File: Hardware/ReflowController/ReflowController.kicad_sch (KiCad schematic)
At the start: 4 parts, among them J1 Conn_01x03_Socket

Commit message: updated main schematic with kerem
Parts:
- removed J1: Conn_01x03_Socket, symbol Connector:Conn_01x03_Socket
- added J10, J11, J3, J4, J5, J6, J7, J8, J9: 2060-1452, 810_connectors_clable_to_Board:wago_2060-1452, symbol Connector:Conn_01x02_Socket
- added J12: RJ45_Display, Connector_RJ:RJ45_Amphenol_54602-x08_Horizontal, symbol Connector:RJ45
- added J13: RJ45_Keypad, Connector_RJ:RJ45_Amphenol_54602-x08_Horizontal, symbol Connector:RJ45
- added J14: Conn_01x03_Socket, 810_connectors_clable_to_Board:wago_2060-1453, symbol Connector:Conn_01x03_Socket
- gave numbers to parts that had none: 3
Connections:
- net PSU/+24V_IN: now also J11.1 (Pin_1)
- net PSU/24V_GND_IN: now also J11.2 (Pin_2)
- net TemperatureReader/PT100_+IN: now also J14.2 (Pin_2)
- net TemperatureReader/PT100_+OUT: now also J14.1 (Pin_1)
- net TemperatureReader/PT100_-IN: now also J14.3 (Pin_3)
- new net Fan Driver/FAN_1_OUT_+: J9.1 (Pin_1)
- new net Fan Driver/FAN_1_OUT_-: J9.2 (Pin_2)
- new net Fan Driver/FAN_2_OUT_+: J10.1 (Pin_1)
- new net Fan Driver/FAN_2_OUT_-: J10.2 (Pin_2)
- new net IO/HSS_1_OUT_+: J3.1 (Pin_1)
- new net IO/HSS_1_OUT_-: J3.2 (Pin_2)
- new net IO/HSS_2_OUT_+: J4.1 (Pin_1)
- new net IO/HSS_2_OUT_-: J5.2 (Pin_2)
- new net IO/HSS_3_OUT_+: J6.1 (Pin_1)
- new net IO/HSS_3_OUT_-: J4.2 (Pin_2)
- new net IO/HSS_4_OUT_+: J5.1 (Pin_1)
- new net IO/HSS_4_OUT_-: J6.2 (Pin_2)
- new net IO/relay_1_coil_+: J7.1 (Pin_1)
- new net IO/relay_1_coil_-: J7.2 (Pin_2)
- new net IO/relay_2_coil_+: J8.1 (Pin_1)
- new net IO/relay_2_coil_-: J8.2 (Pin_2)
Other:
- sheet Fan Driver ports: added +24V, +5V, FAN_1_OUT_+, FAN_1_OUT_-, FAN_2_OUT_+, FAN_2_OUT_-, GND, MOTOR_A_EN, MOTOR_A_PWM, MOTOR_B_EN, MOTOR_B_PWM, PGND; removed FAN+, FAN-
- sheet IO ports: added +3.3V, HSS_1_IN, HSS_1_OUT_+, HSS_1_OUT_-, HSS_1_STATUS, HSS_2_IN, HSS_2_OUT_+, HSS_2_OUT_-, HSS_2_STATUS, HSS_3_IN, HSS_3_OUT_+, HSS_3_OUT_-, HSS_3_STATUS, HSS_4_IN, HSS_4_OUT_+, HSS_4_OUT_-, HSS_4_STATUS, HSS_STATUS_DIS, relay_1_coil_+, relay_1_coil_-, relay_1_in, relay_2_coil_+, relay_2_coil_-, relay_2_in; removed none
- title: (none) -> Reflow Oven Control

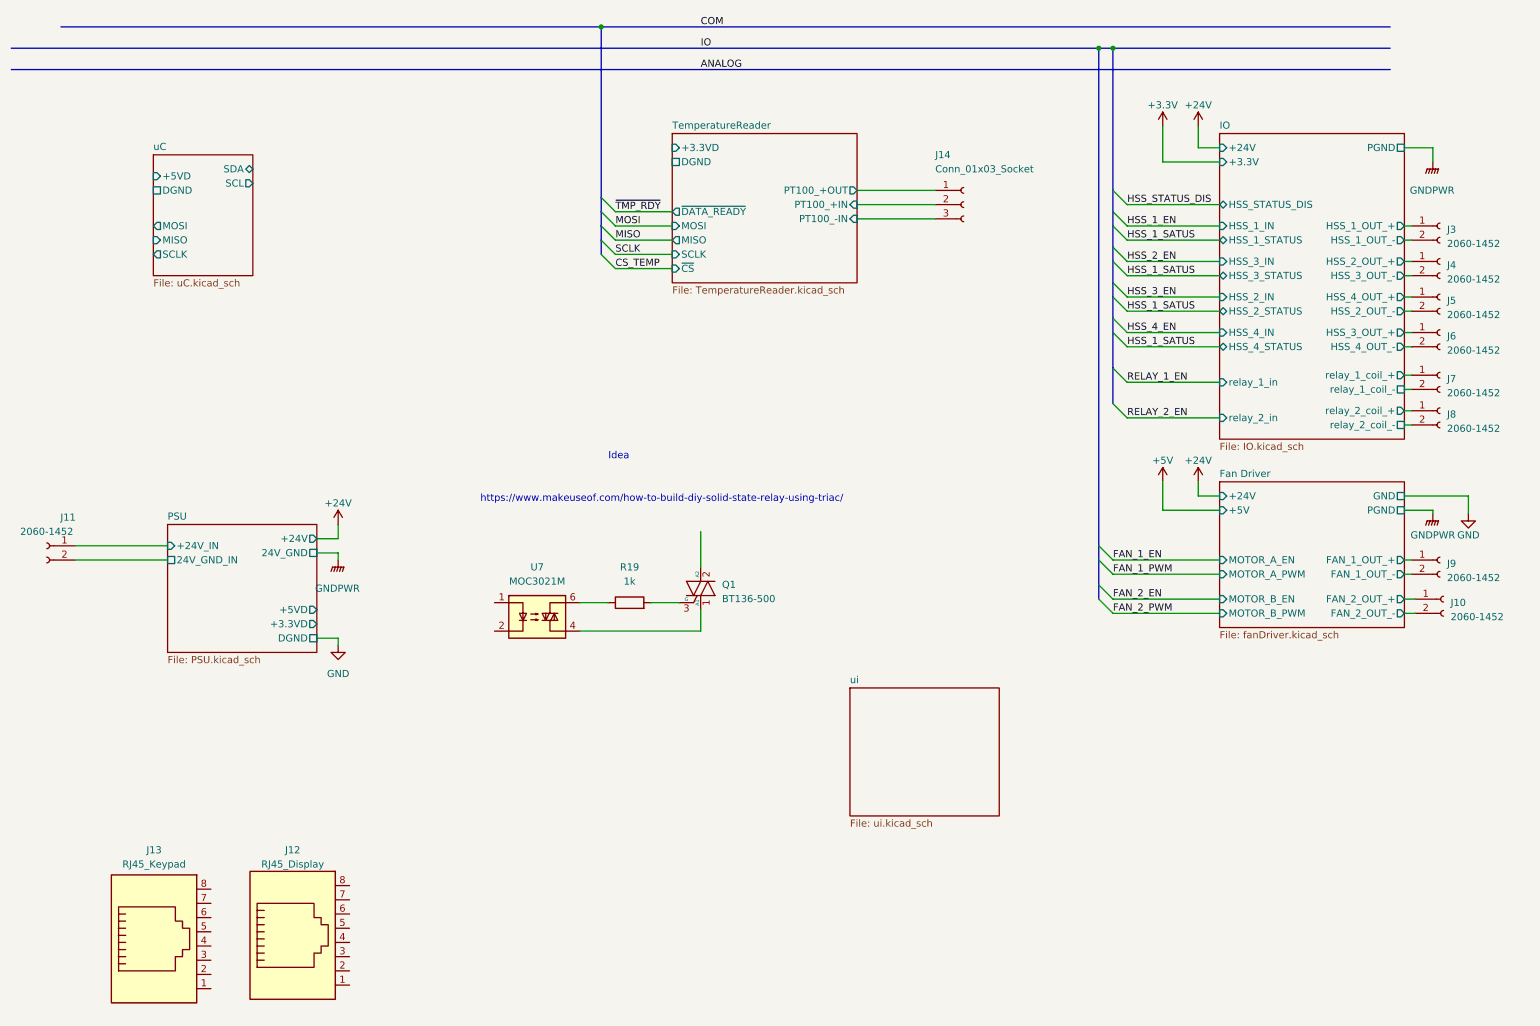
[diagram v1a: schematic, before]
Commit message: added the schematic of the updated pwerAndUi branch(with uC schematic update
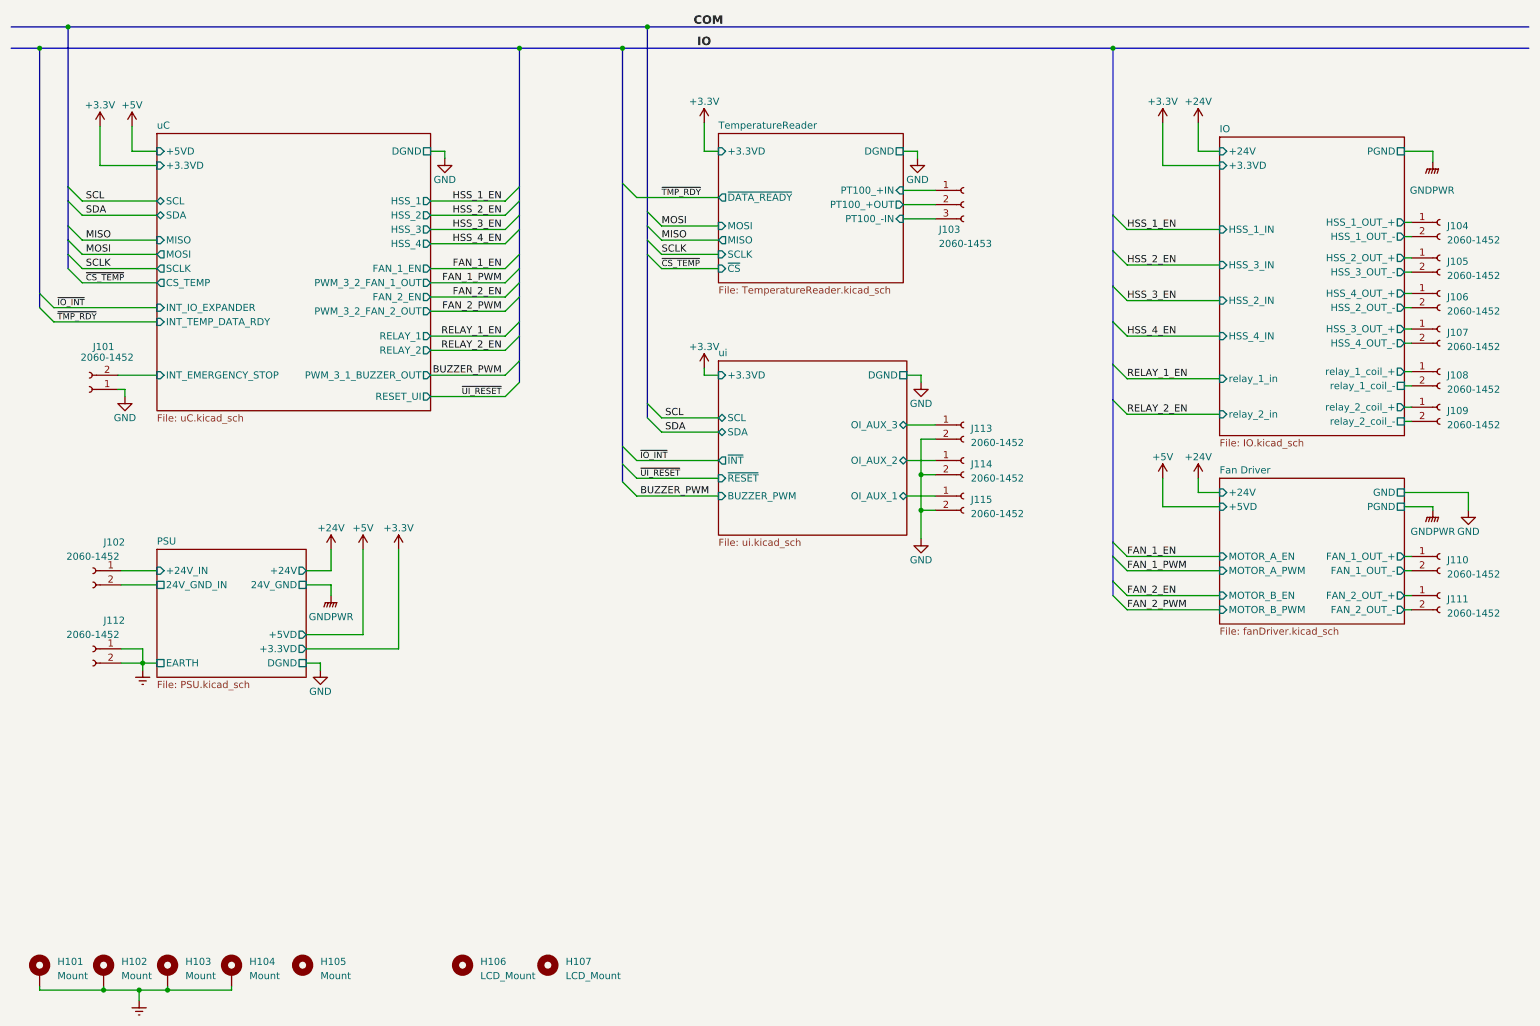
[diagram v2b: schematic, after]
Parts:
- removed J12: RJ45_Display, Connector_RJ:RJ45_Amphenol_54602-x08_Horizontal, symbol Connector:RJ45
- removed J13: RJ45_Keypad, Connector_RJ:RJ45_Amphenol_54602-x08_Horizontal, symbol Connector:RJ45
- removed Q1: BT136-500, Package_TO_SOT_THT:TO-220-3_Vertical, symbol Triac_Thyristor:BT136-500
- removed R19: 1k, Resistor_SMD:R_1206_3216Metric, symbol Device:R
- removed U7: MOC3021M, symbol Relay_SolidState:MOC3021M
- added H101, H102, H103, H104: Mount, MountingHole:MountingHole_3.2mm_M3_Pad_Via, symbol Mechanical:MountingHole_Pad
- added H105: Mount, MountingHole:MountingHole_3.2mm_M3, symbol Mechanical:MountingHole
- added H106, H107: LCD_Mount, MountingHole:MountingHole_2.2mm_M2_ISO7380, symbol Mechanical:MountingHole
- added J101, J112, J113, J114, J115: 2060-1452, 810_connectors_clable_to_Board:wago_2060-1452, symbol Connector:Conn_01x02_Socket
- J103: renamed from J14; value Conn_01x03_Socket -> 2060-1453
- renumbered J11 to J102, J3 to J104, J4 to J105, J5 to J106, J6 to J107, J7 to J108, J8 to J109, J9 to J110, J10 to J111
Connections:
- net GND: now also J101.1 (Pin_1), J113.2 (Pin_2), J114.2 (Pin_2), J115.2 (Pin_2)
- net TemperatureReader/PT100_+IN: now also J103.1 (Pin_1); no longer J103.2 (Pin_2)
- net TemperatureReader/PT100_+OUT: now also J103.2 (Pin_2); no longer J103.1 (Pin_1)
- new net Earth: H101.1, H102.1, H103.1, H104.1, J112.1 (Pin_1), J112.2 (Pin_2)
- new net uC/INT_EMERGENCY_STOP: J101.2 (Pin_2)
- new net ui/OI_AUX_1: J115.1 (Pin_1)
- new net ui/OI_AUX_2: J114.1 (Pin_1)
- new net ui/OI_AUX_3: J113.1 (Pin_1)
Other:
- sheet Fan Driver ports: added +5VD; removed +5V
- sheet IO ports: added +3.3VD; removed +3.3V, HSS_1_STATUS, HSS_2_STATUS, HSS_3_STATUS, HSS_4_STATUS, HSS_STATUS_DIS
- sheet PSU ports: added EARTH; removed none
- sheet uC ports: added +3.3VD, CS_TEMP, FAN_1_EN, FAN_2_EN, HSS_1, HSS_2, HSS_3, HSS_4, INT_EMERGENCY_STOP, INT_IO_EXPANDER, INT_TEMP_DATA_RDY, PWM_3_1_BUZZER_OUT, PWM_3_2_FAN_1_OUT, PWM_3_2_FAN_2_OUT, RELAY_1, RELAY_2, RESET_UI; removed none
- sheet ui ports: added +3.3VD, BUZZER_PWM, DGND, OI_AUX_1, OI_AUX_2, OI_AUX_3, SCL, SDA, ~{INT}, ~{RESET}; removed none
- note removed: "Idea"
- note removed: "https://www.makeuseof.com/how-to-build-diy-solid-state-relay-using-triac/"
- moved on the sheet: J102, J104, J105, J106, J107, J108, J109, J110, J111

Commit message: work on uC circuit. pin selection for the different IOs still pending
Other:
- sheet uC ports: added PWM_BUZZER, PWM_FAN_1, PWM_FAN_2; removed PWM_3_1_BUZZER_OUT, PWM_3_2_FAN_1_OUT, PWM_3_2_FAN_2_OUT
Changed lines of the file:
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@@
       (effects (font (size 1.27 1.27)) (justify left))
     )
-    (pin "PWM_3_1_BUZZER_OUT" output (at 87.63 80.01 0)
+    (pin "PWM_BUZZER" output (at 87.63 80.01 0)
       (effects (font (size 1.27 1.27)) (justify right))
     )
-    (pin "PWM_3_2_FAN_1_OUT" output (at 87.63 63.5 0)
+    (pin "PWM_FAN_1" output (at 87.63 63.5 0)
       (effects (font (size 1.27 1.27)) (justify right))
     )
-    (pin "PWM_3_2_FAN_2_OUT" output (at 87.63 68.58 0)
+    (pin "PWM_FAN_2" output (at 87.63 68.58 0)
       (effects (font (size 1.27 1.27)) (justify right))
     )

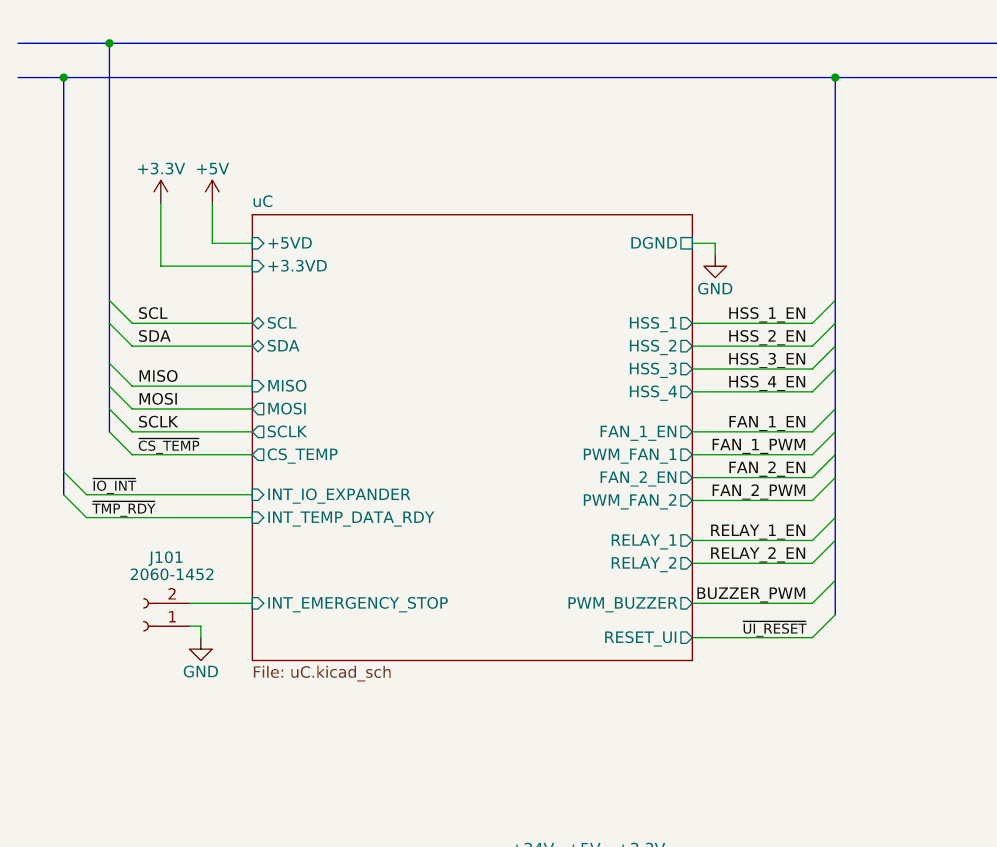
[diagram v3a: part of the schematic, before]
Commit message: work on pin assignment and porttable
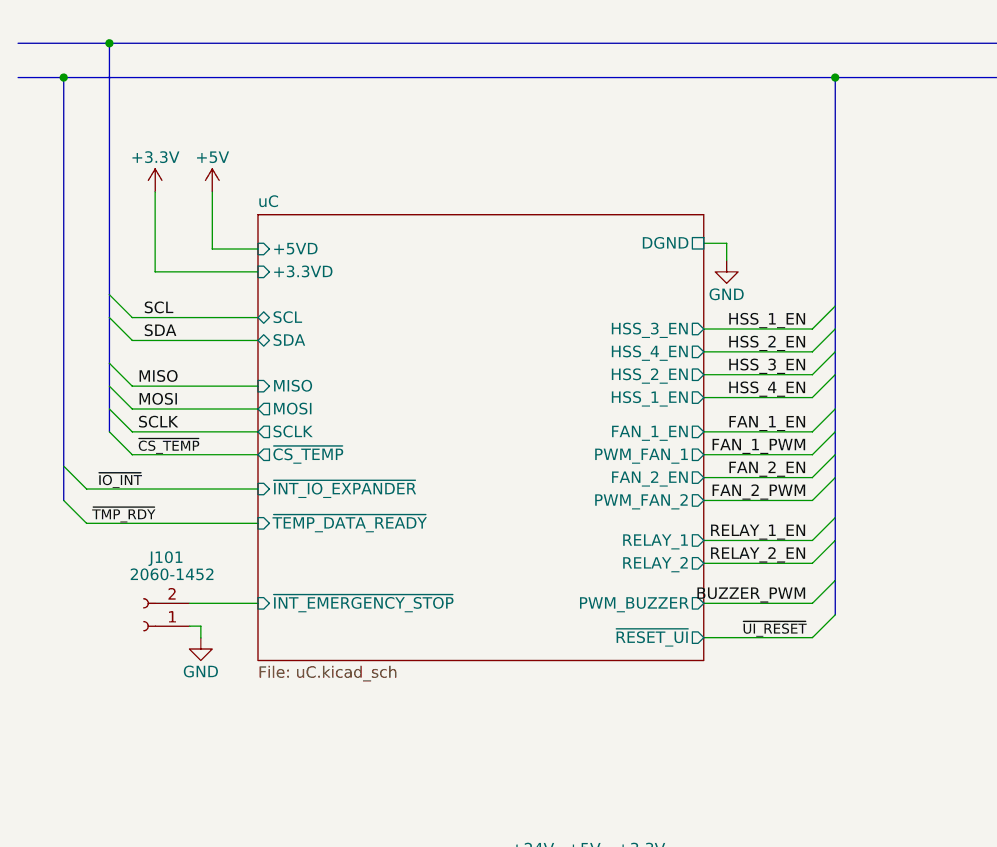
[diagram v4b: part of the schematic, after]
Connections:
- net uC/INT_EMERGENCY_STOP renamed uC/~{INT_EMERGENCY_STOP}
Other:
- sheet uC ports: added HSS_1_EN, HSS_2_EN, HSS_3_EN, HSS_4_EN, ~{CS_TEMP}, ~{INT_EMERGENCY_STOP}, ~{INT_IO_EXPANDER}, ~{RESET_UI}, ~{TEMP_DATA_READY}; removed CS_TEMP, HSS_1, HSS_2, HSS_3, HSS_4, INT_EMERGENCY_STOP, INT_IO_EXPANDER, INT_TEMP_DATA_RDY, RESET_UI

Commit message: work on io adaption
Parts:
- removed J113, J114, J115: 2060-1452, 810_connectors_clable_to_Board:wago_2060-1452, symbol Connector:Conn_01x02_Socket
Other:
- sheet uC ports: added none; removed HSS_1_EN, HSS_2_EN, HSS_3_EN, HSS_4_EN
- sheet ui ports: added OI_AUX_4; removed none
